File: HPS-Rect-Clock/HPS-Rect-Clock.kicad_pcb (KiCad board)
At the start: 2 copper layers, 140 x 90 mm, 52 parts, among them J1 Conn_01x06, J2 Power_inlet_vertical, SW1 Omron_B3F_SPST, SW2 Omron_B3F_SPST, SW3 Omron_B3F_SPST, SW4 Omron_B3F_SPST, SW5 Omron_B3F_SPST, U1 DS1307_DIP-8, U2 ATmega328-PU, U3 L7805, Y1 Crystal_16MHz, Y2 Crystal_32768Hz

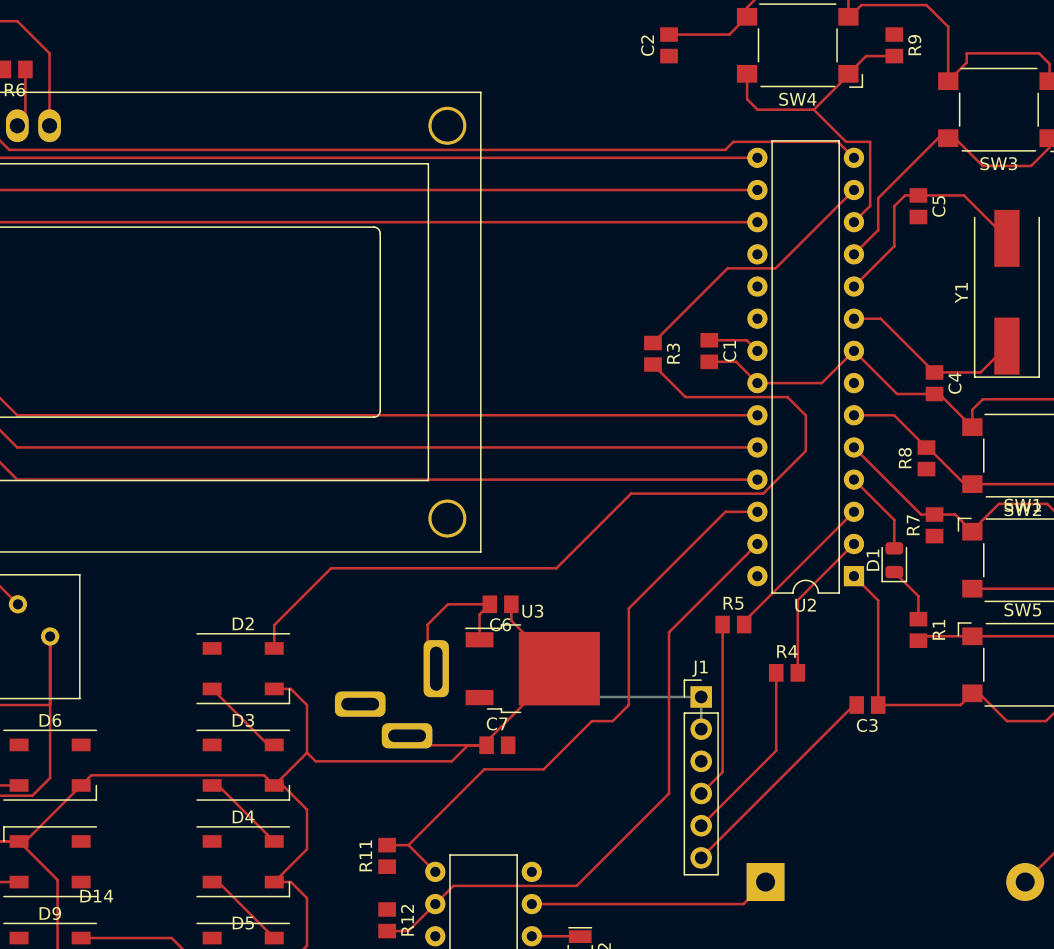
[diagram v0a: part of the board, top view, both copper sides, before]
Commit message: Routing Complete
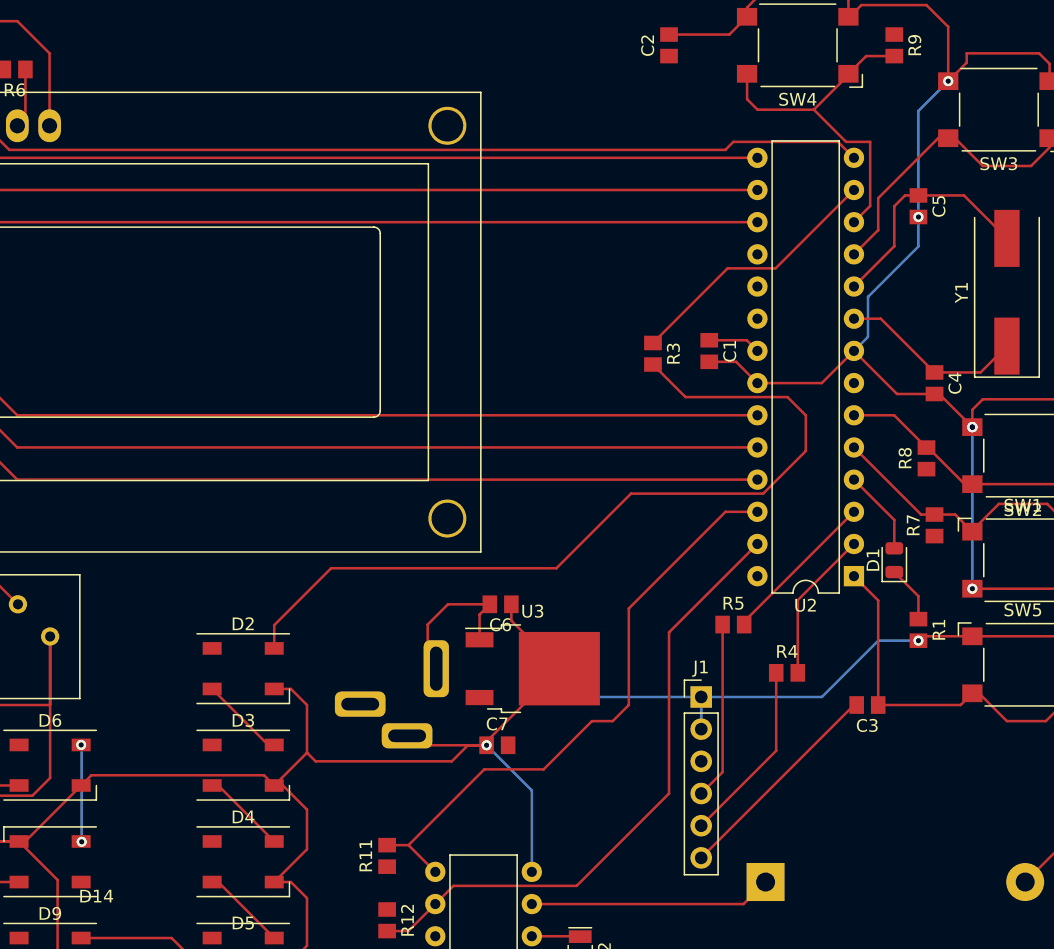
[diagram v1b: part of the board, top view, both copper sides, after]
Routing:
- net GND: track 544.1 -> 611.6 mm, vias 0 -> 7
- net Net-(D14-Pad4): track 0.00 -> 7.72 mm, vias 0 -> 2
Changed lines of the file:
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@@
   (segment (start 82.55 106.045) (end 83.82 107.315) (width 0.2032) (layer "F.Cu") (net 1))
   (segment (start 118.7 129.54) (end 122.555 129.54) (width 0.2032) (layer "F.Cu") (net 1))
+  (via (at 204.28 106.39) (size 0.8128) (drill 0.4064) (layers "F.Cu" "B.Cu") (net 1))
+  (via (at 202.375 66.33) (size 0.8128) (drill 0.4064) (layers "F.Cu" "B.Cu") (net 1))
+  (via (at 165.94 118.745) (size 0.8128) (drill 0.4064) (layers "F.Cu" "B.Cu") (net 1))
+  (via (at 204.28 93.635) (size 0.8128) (drill 0.4064) (layers "F.Cu" "B.Cu") (net 1))
+  (via (at 200.025 110.49) (size 0.8128) (drill 0.4064) (layers "F.Cu" "B.Cu") (net 1))
+  (via (at 204.28 93.635) (size 0.8128) (drill 0.4064) (layers "F.Cu" "B.Cu") (net 1))
+  (via (at 200.025 77.05) (size 0.8128) (drill 0.4064) (layers "F.Cu" "B.Cu") (net 1))
   (segment (start 182.88 114.935) (end 173.355 114.935) (width 0.2032) (layer "B.Cu") (net 1))
+  (segment (start 169.51 128.74) (end 169.51 122.315) (width 0.2032) (layer "B.Cu") (net 1))
+  (segment (start 200.025 68.68) (end 202.375 66.33) (width 0.2032) (layer "B.Cu") (net 1))
+  (segment (start 200.025 79.375) (end 200.025 77.05) (width 0.2032) (layer "B.Cu") (net 1))
+  (segment (start 194.935 87.62) (end 196.0398 86.5152) (width 0.2032) (layer "B.Cu") (net 1))
+  (segment (start 169.51 122.315) (end 165.94 118.745) (width 0.2032) (layer "B.Cu") (net 1))
+  (segment (start 192.405 114.935) (end 196.85 110.49) (width 0.2032) (layer "B.Cu") (net 1))
+  (segment (start 204.28 93.635) (end 204.28 106.39) (width 0.2032) (layer "B.Cu") (net 1))
+  (segment (start 196.85 110.49) (end 200.025 110.49) (width 0.2032) (layer "B.Cu") (net 1))
   (segment (start 173.355 114.935) (end 171.45 113.03) (width 0.2032) (layer "B.Cu") (net 1))
+  (segment (start 182.88 114.935) (end 192.405 114.935) (width 0.2032) (layer "B.Cu") (net 1))
   (segment (start 182.88 114.935) (end 182.88 117.475) (width 0.2032) (layer "B.Cu") (net 1))
+  (segment (start 196.0398 86.5152) (end 196.0398 83.3602) (width 0.2032) (layer "B.Cu") (net 1))
+  (segment (start 196.0398 83.3602) (end 200.025 79.375) (width 0.2032) (layer "B.Cu") (net 1))
+  (segment (start 200.025 77.05) (end 200.025 68.68) (width 0.2032) (layer "B.Cu") (net 1))
   (segment (start 186.22 131.28) (end 187.96 129.54) (width 0.2032) (layer "F.Cu") (net 2))
   (segment (start 169.51 131.28) (end 186.22 131.28) (width 0.2032) (layer "F.Cu") (net 2))
@@
   (segment (start 141.08 133.96) (end 144.28 137.16) (width 0.2032) (layer "F.Cu") (net 16))
   (segment (start 133.94 133.96) (end 141.08 133.96) (width 0.2032) (layer "F.Cu") (net 16))
+  (segment (start 133.96 126.34) (end 133.985 126.365) (width 0.2032) (layer "F.Cu") (net 17))
+  (segment (start 133.94 126.34) (end 133.96 126.34) (width 0.2032) (layer "F.Cu") (net 17))
+  (via (at 133.985 126.365) (size 0.8128) (drill 0.4064) (layers "F.Cu" "B.Cu") (net 17))
+  (via (at 133.94 118.72) (size 0.8128) (drill 0.4064) (layers "F.Cu" "B.Cu") (net 17))
+  (segment (start 133.985 126.365) (end 133.985 118.765) (width 0.2032) (layer "B.Cu") (net 17))
+  (segment (start 133.985 118.765) (end 133.94 118.72) (width 0.2032) (layer "B.Cu") (net 17))
   (segment (start 121.92 121.92) (end 129.04 121.92) (width 0.2032) (layer "F.Cu") (net 18))
   (segment (start 121.92 114.935) (end 121.92 121.92) (width 0.2032) (layer "F.Cu") (net 18))

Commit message: GND and vertical and horizontal
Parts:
- added TP1: TestPoint, footprints:TestPoint_THTPad_D2.0mm_Drill1.0mm, F.Cu at (175.5, 87.0)
- moved RV1 58.8 mm to (100.3, 60.3), turned to 180 degrees
- moved R6 7.45 mm to (135.9, 67.3), turned to 90 degrees
- moved DS1 5.75 mm to (98.8, 71.6)
- moved C5 3.52 mm to (202.6, 78.6)
- moved R9 1.62 mm to (197.4, 65.0)
- moved R10 1.42 mm to (214.0, 70.0)
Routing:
- net GND: track 611.6 -> 76.8 mm, vias 7 -> 29
- net Net-(DS1-Pad3): track 50.4 -> 11.3 mm
- net SW4: track 28.1 -> 39.9 mm, vias 0 -> 4
- net NEO: track 66.0 -> 54.3 mm, vias 0 -> 2
- net RS: track 97.9 -> 106.8 mm, vias 0 -> 1
- net SCL: track 49.3 -> 57.8 mm, vias 0 -> 6
- net SDA: track 47.6 -> 55.7 mm, vias 0 -> 4
- net Net-(D14-Pad4): track 7.72 -> 0.00 mm, vias 2 -> 0
- net RW: track 94.3 -> 101.2 mm, vias 0 -> 1
- net Net-(C3-Pad2): track 17.3 -> 23.8 mm, vias 0 -> 2
- net Net-(R3-Pad1): track 20.9 -> 27.3 mm, vias 0 -> 4
- net Net-(J1-Pad4): track 14.0 -> 20.3 mm, vias 0 -> 2
- net D4: track 71.7 -> 65.5 mm
- net D5: track 68.1 -> 61.9 mm
- net E: track 90.7 -> 96.7 mm, vias 0 -> 1
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- removed copper zone on B.Cu, net GND

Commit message: test points added
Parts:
- added TP2: TestPoint, footprints:TestPoint_THTPad_D2.0mm_Drill1.0mm, F.Cu at (212.8, 83.0)
- added TP3: TestPoint, footprints:TestPoint_THTPad_D2.0mm_Drill1.0mm, F.Cu at (200.6, 74.6)
- added TP4: TestPoint, footprints:TestPoint_THTPad_D2.0mm_Drill1.0mm, F.Cu at (178.4, 69.0)
- added TP5: TestPoint, footprints:TestPoint_THTPad_D2.0mm_Drill1.0mm, F.Cu at (215.6, 99.0)
- added TP6: TestPoint, footprints:TestPoint_THTPad_D2.0mm_Drill1.0mm, F.Cu at (213.8, 89.8)
- moved TP1 3.83 mm to (175.0, 83.2)
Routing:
- net NEO: track 54.3 -> 58.2 mm, vias 2 -> 3
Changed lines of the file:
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@@
     )
+  )
+  (footprint "footprints:TestPoint_THTPad_D2.0mm_Drill1.0mm" (layer "F.Cu")
+    (at 213.8 89.8)
+    (descr "THT pad as test Point, diameter 2.0mm, hole diameter 1.0mm")
+    (tags "test point THT pad")
+    (property "Sheetfile" "HPS-Rect-Clock.kicad_sch")
+    (property "Sheetname" "")
+    (attr exclude_from_pos_files)
+    (fp_text reference "TP6" (at 0 -1.998) (layer "F.SilkS")
+      (effects (font (size 1 1) (thickness 0.15)))
+    )
+    (fp_text value "TestPoint" (at 0 2.05) (layer "F.Fab")
+      (effects (font (size 1 1) (thickness 0.15)))
+    )
+    (fp_text user "${REFERENCE}" (at 0 -2) (layer "F.Fab")
+      (effects (font (size 1 1) (thickness 0.15)))
+    )
+    (fp_circle (center 0 0) (end 0 1.2) (layer "F.SilkS") (width 0.12) (fill none))
+    (fp_circle (center 0 0) (end 1.5 0) (layer "F.CrtYd") (width 0.05) (fill none))
+    (pad "1" thru_hole circle (at 0 0) (size 2 2) (drill 1) (layers *.Cu *.Mask)
+      (net 47 "SW2") (pinfunction "1") (pintype "passive"))
   )
   (footprint "footprints:LED_SK6812_PLCC4_5.0x5.0mm_P3.2mm" (layer "F.Cu")
@@
     )
   )
+  (footprint "footprints:TestPoint_THTPad_D2.0mm_Drill1.0mm" (layer "F.Cu")
+    (at 178.4 69)
+    (descr "THT pad as test Point, diameter 2.0mm, hole diameter 1.0mm")
+    (tags "test point THT pad")
+    (property "Sheetfile" "HPS-Rect-Clock.kicad_sch")
+    (property "Sheetname" "")
+    (attr exclude_from_pos_files)
+    (fp_text reference "TP4" (at 0 -1.998) (layer "F.SilkS")
+      (effects (font (size 1 1) (thickness 0.15)))
+    )
+    (fp_text value "TestPoint" (at 0 2.05) (layer "F.Fab")
+      (effects (font (size 1 1) (thickness 0.15)))
+    )
+    (fp_text user "${REFERENCE}" (at 0 -2) (layer "F.Fab")
+      (effects (font (size 1 1) (thickness 0.15)))
+    )
+    (fp_circle (center 0 0) (end 0 1.2) (layer "F.SilkS") (width 0.12) (fill none))
+    (fp_circle (center 0 0) (end 1.5 0) (layer "F.CrtYd") (width 0.05) (fill none))
+    (pad "1" thru_hole circle (at 0 0) (size 2 2) (drill 1) (layers *.Cu *.Mask)
+      (net 48 "SW4") (pinfunction "1") (pintype "passive"))
+  )
   (footprint "footprints:Crystal_SMD_HC49-SD" (layer "F.Cu")
     (at 207.01 82.99 90)
@@
     (fp_circle (center 0 0) (end 3.45 0) (layer "F.CrtYd") (width 0.05) (fill none))
     (pad "" np_thru_hole circle locked (at 0 0) (size 3.2 3.2) (drill 3.2) (layers *.Cu *.Mask))
+  )
+  (footprint "footprints:TestPoint_THTPad_D2.0mm_Drill1.0mm" (layer "F.Cu")
+    (at 215.6 99)
+    (descr "THT pad as test Point, diameter 2.0mm, hole diameter 1.0mm")
+    (tags "test point THT pad")
+    (property "Sheetfile" "HPS-Rect-Clock.kicad_sch")
+    (property "Sheetname" "")
+    (attr exclude_from_pos_files)
+    (fp_text reference "TP5" (at 0 -1.998) (layer "F.SilkS")
+      (effects (font (size 1 1) (thickness 0.15)))
+    )
+    (fp_text value "TestPoint" (at 0 2.05) (layer "F.Fab")
+      (effects (font (size 1 1) (thickness 0.15)))
+    )
+    (fp_text user "${REFERENCE}" (at 0 -2) (layer "F.Fab")
+      (effects (font (size 1 1) (thickness 0.15)))
+    )
+    (fp_circle (center 0 0) (end 0 1.2) (layer "F.SilkS") (width 0.12) (fill none))
+    (fp_circle (center 0 0) (end 1.5 0) (layer "F.CrtYd") (width 0.05) (fill none))
+    (pad "1" thru_hole circle (at 0 0) (size 2 2) (drill 1) (layers *.Cu *.Mask)
+      (net 46 "SW1") (pinfunction "1") (pintype "passive"))
   )
   (footprint "footprints:LED_SK6812_PLCC4_5.0x5.0mm_P3.2mm" (layer "F.Cu")
@@
   )
   (footprint "footprints:TestPoint_THTPad_D2.0mm_Drill1.0mm" (layer "F.Cu")
-    (at 175.5 87)
+    (at 175 83.2)
     (descr "THT pad as test Point, diameter 2.0mm, hole diameter 1.0mm")
     (tags "test point THT pad")
@@
     )
   )
+  (footprint "footprints:TestPoint_THTPad_D2.0mm_Drill1.0mm" (layer "F.Cu")
+    (at 200.6 74.6)
+    (descr "THT pad as test Point, diameter 2.0mm, hole diameter 1.0mm")
+    (tags "test point THT pad")
+    (property "Sheetfile" "HPS-Rect-Clock.kicad_sch")
+    (property "Sheetname" "")
+    (attr exclude_from_pos_files)
+    (fp_text reference "TP3" (at 0 -1.998) (layer "F.SilkS")
+      (effects (font (size 1 1) (thickness 0.15)))
+    )
+    (fp_text value "TestPoint" (at 0 2.05) (layer "F.Fab")
+      (effects (font (size 1 1) (thickness 0.15)))
+    )
+    (fp_text user "${REFERENCE}" (at 0 -2) (layer "F.Fab")
+      (effects (font (size 1 1) (thickness 0.15)))
+    )
+    (fp_circle (center 0 0) (end 0 1.2) (layer "F.SilkS") (width 0.12) (fill none))
+    (fp_circle (center 0 0) (end 1.5 0) (layer "F.CrtYd") (width 0.05) (fill none))
+    (pad "1" thru_hole circle (at 0 0) (size 2 2) (drill 1) (layers *.Cu *.Mask)
+      (net 49 "SW3") (pinfunction "1") (pintype "passive"))
+  )
   (footprint "footprints:LED_0805_2012Metric" (layer "F.Cu")
     (at 198.12 104.14 90)
@@
       (rotate (xyz 0 0 0))
     )
+  )
+  (footprint "footprints:TestPoint_THTPad_D2.0mm_Drill1.0mm" (layer "F.Cu")
+    (at 212.8 83)
+    (descr "THT pad as test Point, diameter 2.0mm, hole diameter 1.0mm")
+    (tags "test point THT pad")
+    (property "Sheetfile" "HPS-Rect-Clock.kicad_sch")
+    (property "Sheetname" "")
+    (attr exclude_from_pos_files)
+    (fp_text reference "TP2" (at 0 -1.998) (layer "F.SilkS")
+      (effects (font (size 1 1) (thickness 0.15)))
+    )
+    (fp_text value "TestPoint" (at 0 2.05) (layer "F.Fab")
+      (effects (font (size 1 1) (thickness 0.15)))
+    )
+    (fp_text user "${REFERENCE}" (at 0 -2) (layer "F.Fab")
+      (effects (font (size 1 1) (thickness 0.15)))
+    )
+    (fp_circle (center 0 0) (end 0 1.2) (layer "F.SilkS") (width 0.12) (fill none))
+    (fp_circle (center 0 0) (end 1.5 0) (layer "F.CrtYd") (width 0.05) (fill none))
+    (pad "1" thru_hole circle (at 0 0) (size 2 2) (drill 1) (layers *.Cu *.Mask)
+      (net 7 "Net-(C4-Pad1)") (pinfunction "1") (pintype "passive"))
   )
   (footprint "footprints:C_0805_2012Metric" (layer "F.Cu")
@@
   (via (at 196.6 103.2) (size 0.8128) (drill 0.4064) (layers "F.Cu" "B.Cu") (net 11))
   (segment (start 196.6 103.2) (end 196.6 98) (width 0.2032) (layer "B.Cu") (net 11))
-  (segment (start 159.2 87) (end 175.5 87) (width 0.2032) (layer "F.Cu") (net 12))
-  (segment (start 175.5 87) (end 177.195 88.695) (width 0.2032) (layer "F.Cu") (net 12))
-  (segment (start 177.195 88.695) (end 179.07 88.695) (width 0.2032) (layer "F.Cu") (net 12))
+  (segment (start 174.8 87.4) (end 175.2 87) (width 0.2032) (layer "F.Cu") (net 12))
   (segment (start 158.353734 111.1) (end 158.96642 110.487314) (width 0.2032) (layer "F.Cu") (net 12))
   (segment (start 149.18 111.1) (end 158.353734 111.1) (width 0.2032) (layer "F.Cu") (net 12))
-  (segment (start 158.8 87.4) (end 159.2 87) (width 0.2032) (layer "F.Cu") (net 12))
+  (segment (start 158.8 87.4) (end 174.8 87.4) (width 0.2032) (layer "F.Cu") (net 12))
+  (segment (start 175.2 87) (end 176.895 88.695) (width 0.2032) (layer "F.Cu") (net 12))
+  (segment (start 176.895 88.695) (end 179.07 88.695) (width 0.2032) (layer "F.Cu") (net 12))
   (via (at 158.96642 110.487314) (size 0.8128) (drill 0.4064) (layers "F.Cu" "B.Cu") (net 12))
   (via (at 158.8 87.4) (size 0.8128) (drill 0.4064) (layers "F.Cu" "B.Cu") (net 12))
+  (via (at 175.2 87) (size 0.8128) (drill 0.4064) (layers "F.Cu" "B.Cu") (net 12))
+  (segment (start 175 86.8) (end 175.2 87) (width 0.2032) (layer "B.Cu") (net 12))
   (segment (start 158.8 110.320894) (end 158.8 87.4) (width 0.2032) (layer "B.Cu") (net 12))
+  (segment (start 175 83.2) (end 175 86.8) (width 0.2032) (layer "B.Cu") (net 12))
   (segment (start 158.96642 110.487314) (end 158.8 110.320894) (width 0.2032) (layer "B.Cu") (net 12))
   (segment (start 148.7 118.72) (end 149.18 118.72) (width 0.2032) (layer "F.Cu") (net 13))

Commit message: Pre Gerber Edits
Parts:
- removed TP2: TestPoint, footprints:TestPoint_THTPad_D2.0mm_Drill1.0mm
- added J3: Conn_02x03_Odd_Even, footprints:PinHeader_2x03_P2.54mm_Vertical, B.Cu at (159.7, 65.2)
- moved TP6 6.25 mm to (214.6, 96.0)
- moved R8 1.88 mm to (201.8, 97.6), turned to -90 degrees
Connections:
- U2 pad 17: D4 -> MOSI
- U2 pad 18: unconnected-(U2-Pad18) -> MISO
- U2 pad 19: unconnected-(U2-Pad19) -> ICSP_SCK
- U2 pad 28: unconnected-(U2-Pad28) -> D4
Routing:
- net RESET: track 31.0 -> 112.4 mm, vias 0 -> 1
- net ICSP_SCK: track 0.00 -> 46.4 mm, vias 0 -> 1
- net MOSI: track 0.00 -> 44.1 mm, vias 0 -> 2
- net MISO: track 0.00 -> 42.2 mm, vias 0 -> 2
- net D4: track 65.5 -> 96.1 mm, vias 0 -> 1
- net SW4: track 39.9 -> 45.3 mm
- net SW1: track 23.0 -> 27.6 mm
- net SW3: track 28.9 -> 33.5 mm
- net SW2: vias 4 -> 0
- added copper zone on B.Cu, net GND

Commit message: PreGerber Edits
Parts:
- moved R6 0.33 mm to (136.0, 67.0)
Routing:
- net Net-(D14-Pad4): track 0.00 -> 16.2 mm, vias 0 -> 2
- net Net-(DS1-Pad15): track 0.00 -> 4.46 mm
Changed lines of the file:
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@@
   )
   (footprint "footprints:R_0805_2012Metric" (layer "F.Cu")
-    (at 135.89 67.31 90)
+    (at 136 67 90)
     (descr "Resistor SMD 0805 (2012 Metric), square (rectangular) end terminal, IPC_7351 nominal, (Body size source: http://www.tortai-tech.com/upload/download/2011102023233369053.pdf), generated with kicad-footprint-generator")
     (tags "resistor")
@@
   (segment (start 141.08 133.96) (end 144.28 137.16) (width 0.2032) (layer "F.Cu") (net 16))
   (segment (start 133.94 133.96) (end 141.08 133.96) (width 0.2032) (layer "F.Cu") (net 16))
+  (segment (start 133.94 118.72) (end 138.12 118.72) (width 0.2032) (layer "F.Cu") (net 17))
+  (segment (start 138.14 126.34) (end 133.94 126.34) (width 0.2032) (layer "F.Cu") (net 17))
+  (segment (start 138.12 118.72) (end 138.2 118.8) (width 0.2032) (layer "F.Cu") (net 17))
+  (segment (start 138.2 126.4) (end 138.14 126.34) (width 0.2032) (layer "F.Cu") (net 17))
+  (via (at 138.2 118.8) (size 0.8128) (drill 0.4064) (layers "F.Cu" "B.Cu") (net 17))
+  (via (at 138.2 126.4) (size 0.8128) (drill 0.4064) (layers "F.Cu" "B.Cu") (net 17))
+  (segment (start 138.2 118.8) (end 138.2 126.4) (width 0.2032) (layer "B.Cu") (net 17))
   (segment (start 121.92 121.92) (end 129.04 121.92) (width 0.2032) (layer "F.Cu") (net 18))
   (segment (start 121.92 114.935) (end 121.92 121.92) (width 0.2032) (layer "F.Cu") (net 18))
@@
   (segment (start 98.56 129.54) (end 96.52 129.54) (width 0.2032) (layer "F.Cu") (net 24))
   (segment (start 93.98 132.58) (end 98.56 137.16) (width 0.2032) (layer "F.Cu") (net 24))
+  (segment (start 136 70.0075) (end 134.37 71.6375) (width 0.2032) (layer "F.Cu") (net 26))
+  (segment (start 136 67.85) (end 136 70.0075) (width 0.2032) (layer "F.Cu") (net 26))
   (segment (start 167.562427 73.4423) (end 181.1927 73.4423) (width 0.2032) (layer "F.Cu") (net 27))
   (segment (start 133.464937 73.272437) (end 167.392564 73.272437) (width 0.2032) (layer "F.Cu") (net 27))

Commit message: Pre Gerber Edits  - DRC
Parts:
- moved C4 7.64 mm to (208.2, 87.0), turned to 0 degrees
- moved C5 5.41 mm to (208.0, 79.0), turned to 0 degrees
- moved Y1 4.25 mm to (202.8, 83.6)
- moved R12 1.35 mm to (159.4, 132.2), turned to 90 degrees
- moved BT1 0.58 mm to (187.6, 130.0)
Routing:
- net SCL: track 57.8 -> 50.0 mm, vias 6 -> 3
- net GND: track 76.8 -> 81.4 mm, vias 29 -> 31
- net Net-(C5-Pad1): track 17.2 -> 13.7 mm, vias 2 -> 0
- net Net-(C4-Pad1): track 17.4 -> 14.0 mm, vias 2 -> 0
- net SDA: track 55.7 -> 58.7 mm
- net Net-(C3-Pad2): track 23.8 -> 23.2 mm, vias 2 -> 1
- net Net-(BT1-Pad1): track 19.2 -> 18.6 mm
